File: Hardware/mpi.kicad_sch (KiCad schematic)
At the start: 26 parts, among them J22 J-0530471010, J23 J-0532610471, U6 U-MAX3378EEUD+T, U7 MAX3086EESD+T, U8 THVD1406DR

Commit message: Memory
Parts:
- removed R91, R92, R93, R94, R95: 100K, Resistor_SMD:R_0603_1608Metric, symbol OBC Development Board:root_0_RT-100K0-F-1/16W-0603_OBC Development Board.SchLib
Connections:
- no-connect marks 0 -> 5

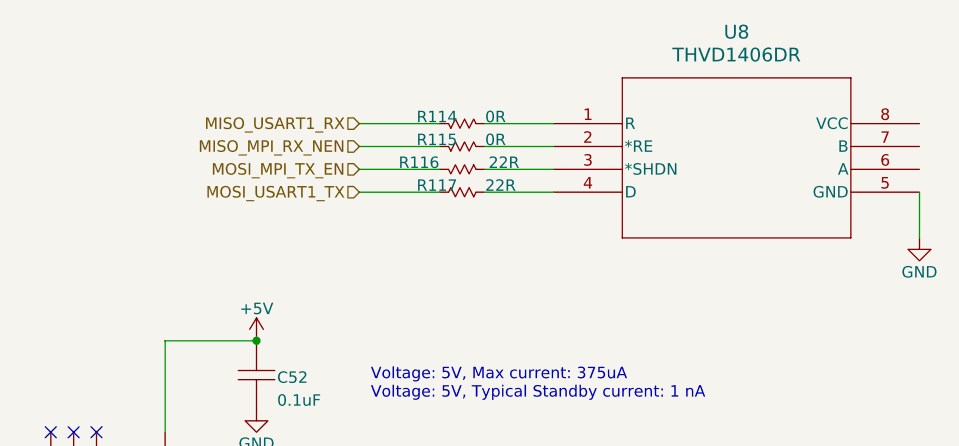
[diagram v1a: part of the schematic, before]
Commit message: MPI layout
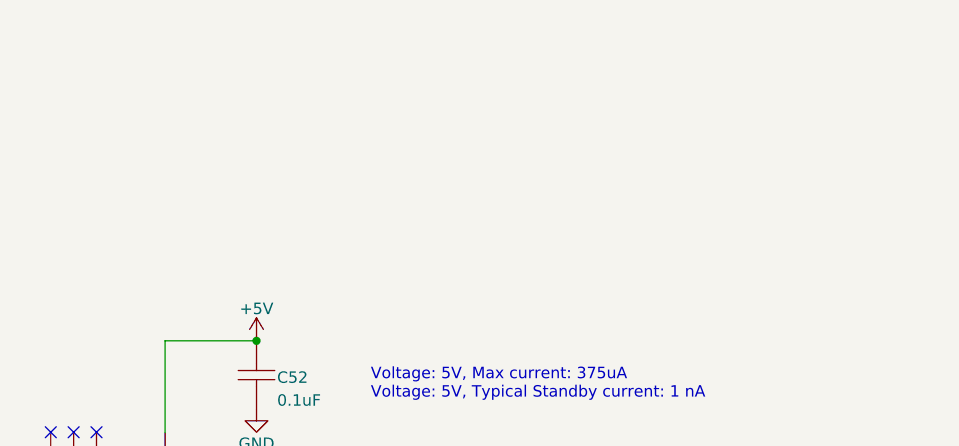
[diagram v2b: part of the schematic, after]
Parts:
- removed R114, R115: 0R, Resistor_SMD:R_0603_1608Metric, symbol OBC Development Board:root_0_RT-0R00-F-1/10W-0603_OBC Development Board.SchLib
- removed R116: 22R, Resistor_SMD:R_0603_1608Metric, symbol OBC Development Board:root_2_mirrored_RT-22R0-F-1/16W-0603_OBC Development Boar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
- removed R117: 22R, Resistor_SMD:R_0603_1608Metric, symbol OBC Development Board:root_0_mirrored_RT-22R0-F-1/16W-0603_OBC Development Boar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
- removed U8: THVD1406DR, SOIC_D0008A_TEX, symbol THVD1406DR:THVD1406DR

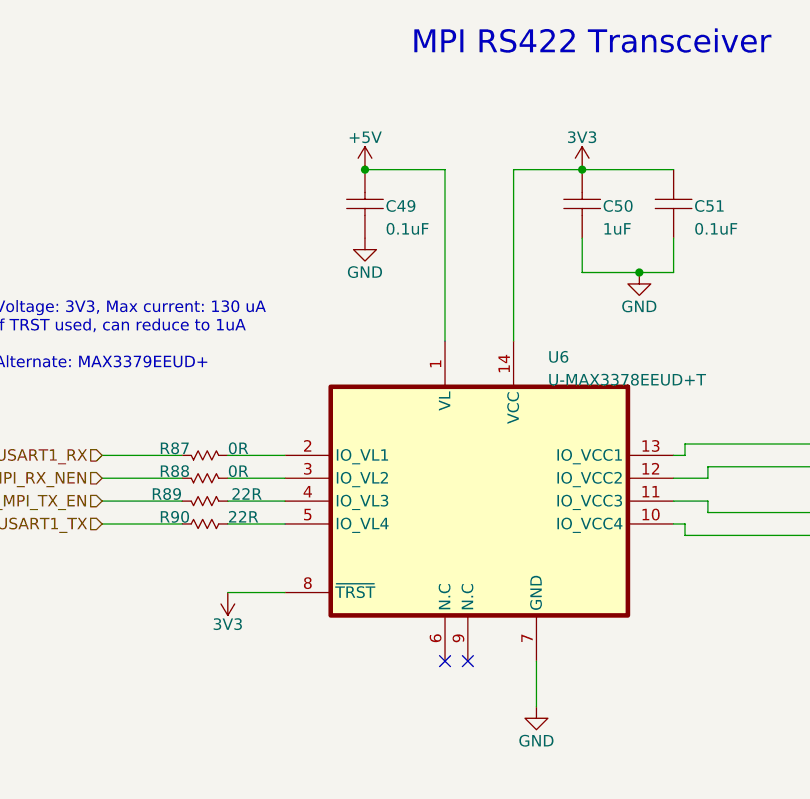
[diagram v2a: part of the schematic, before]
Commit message: Reroute power
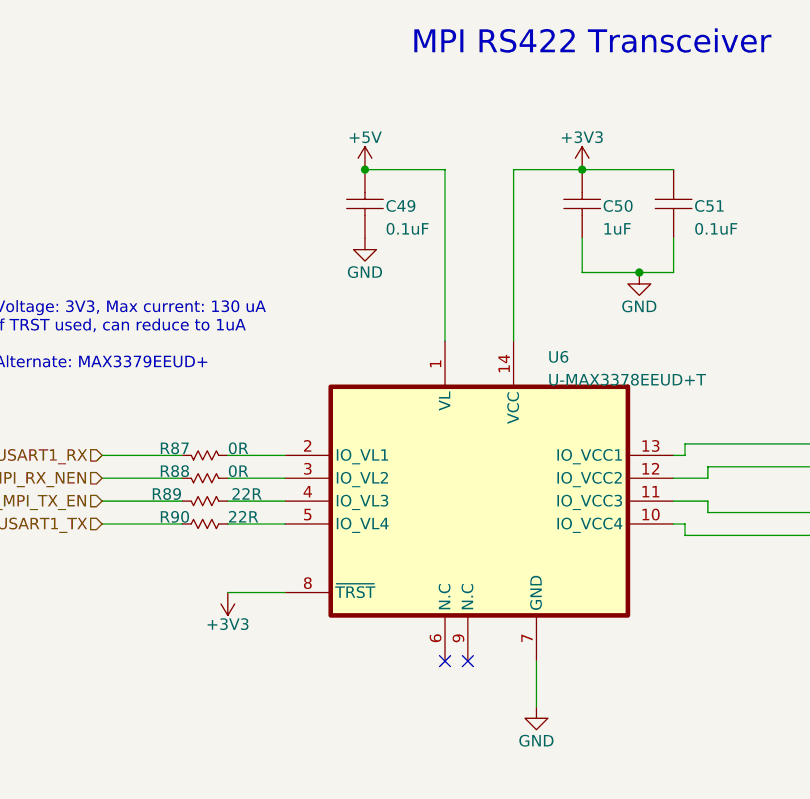
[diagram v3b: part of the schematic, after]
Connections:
- net 3V3 renamed +3V3
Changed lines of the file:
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@@
 			)
 		)
-		(property "Value" "3V3"
+		(property "Value" "+3V3"
 			(at 120.65 48.514 0)
 			(effects
@@
 			)
 		)
-		(property "Value" "3V3"
+		(property "Value" "+3V3"
 			(at 81.28 102.616 0)
 			(effects
